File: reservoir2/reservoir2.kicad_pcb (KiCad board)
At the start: 2 copper layers, 104.1 x 66.7 mm, 2 parts

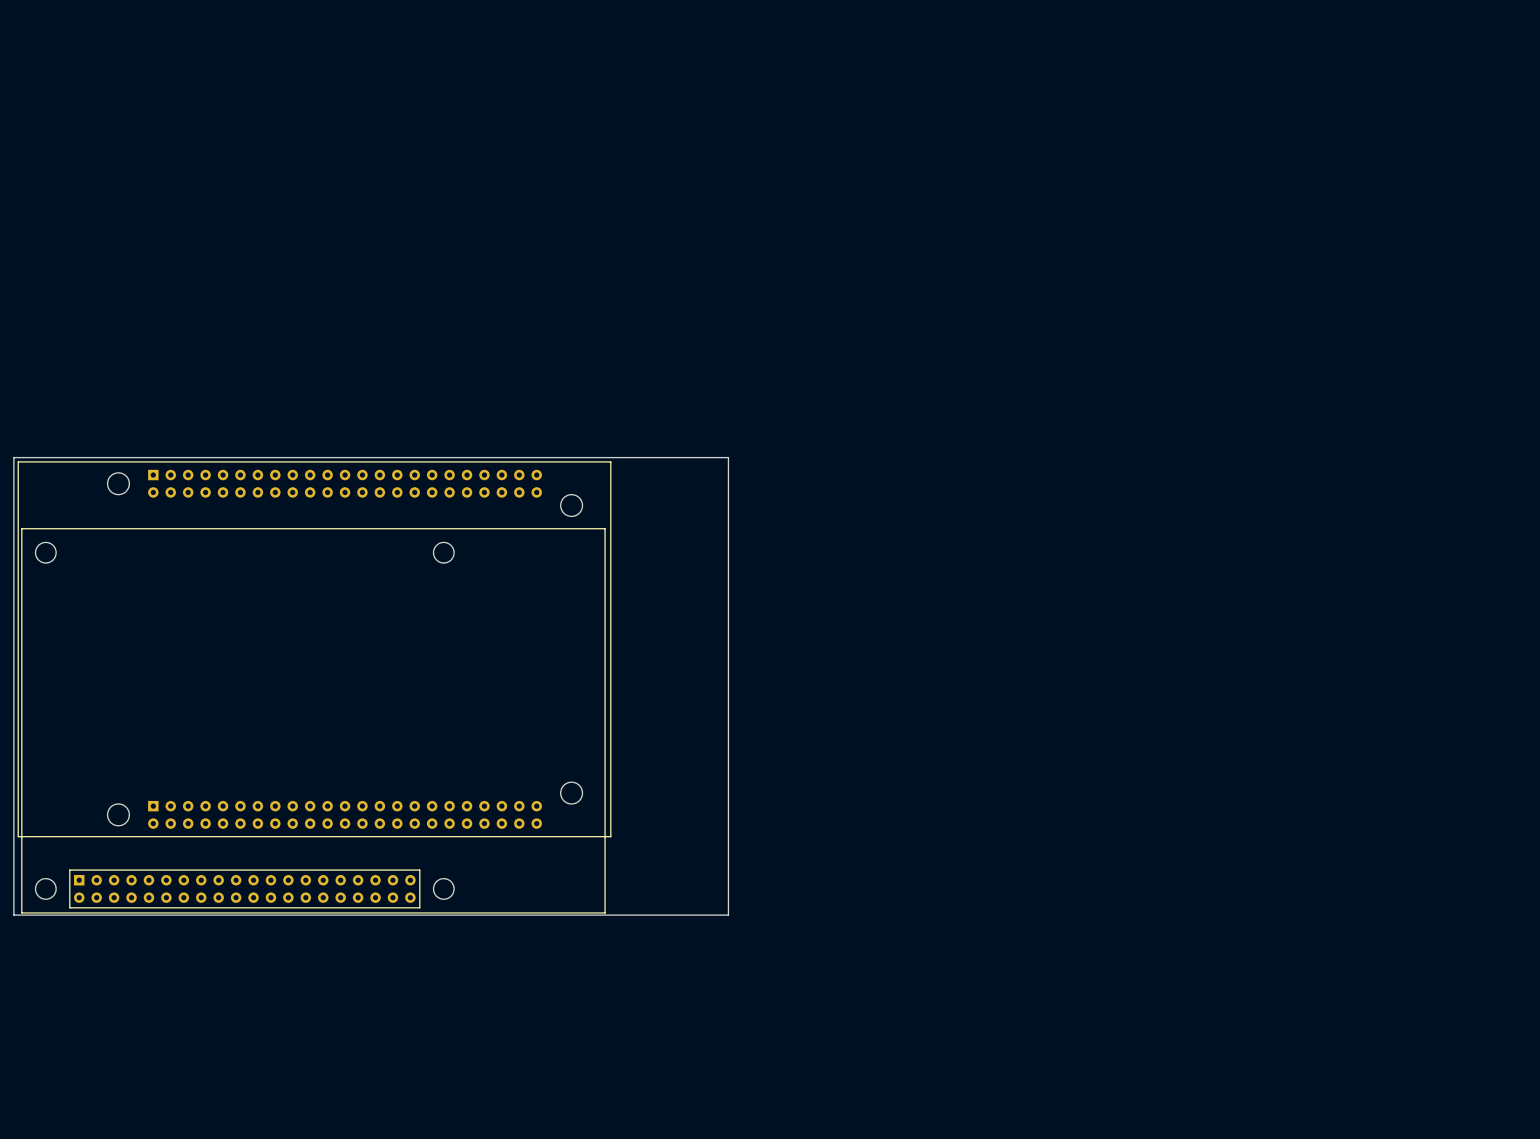
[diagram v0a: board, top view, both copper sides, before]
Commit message: Created new board design for connected grounds.
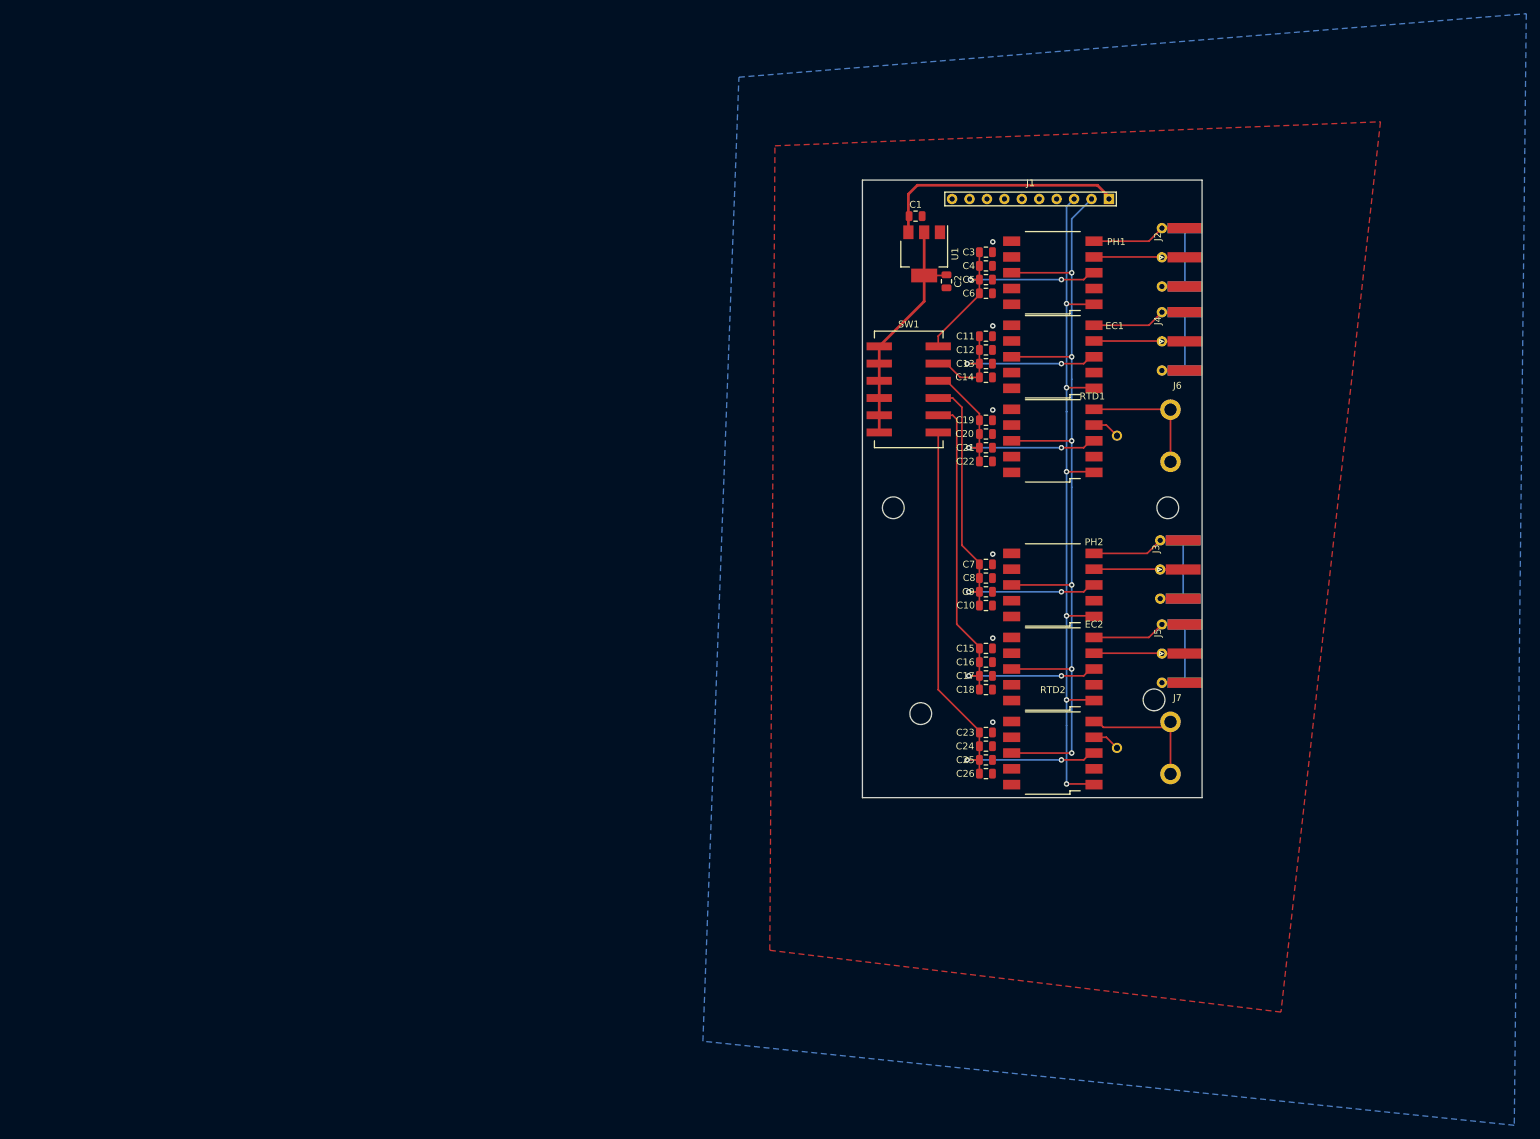
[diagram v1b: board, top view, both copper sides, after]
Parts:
- removed REF**: RaspberryPi_UpsideDown, BCR_SBC:RaspberryPi_UpsideDown
- removed REF**: BeagleBone_UpsideDown, BCR_SBC:BeagleBone_UpsideDown
- added C1: 0.1uF, Capacitor_SMD:C_0805_2012Metric, F.Cu at (208.2, 24.5)
- added C10: 0.1uF, Capacitor_SMD:C_0805_2012Metric, F.Cu at (218.5, 81.2)
- added C11: 0.1uF, Capacitor_SMD:C_0805_2012Metric, F.Cu at (218.5, 42.0)
- added C12: 0.1uF, Capacitor_SMD:C_0805_2012Metric, F.Cu at (218.5, 44.0)
- added C13: 0.1uF, Capacitor_SMD:C_0805_2012Metric, F.Cu at (218.5, 46.0)
- added C14: 0.1uF, Capacitor_SMD:C_0805_2012Metric, F.Cu at (218.5, 48.0)
- added C15: 0.1uF, Capacitor_SMD:C_0805_2012Metric, F.Cu at (218.5, 87.5)
- added C16: 0.1uF, Capacitor_SMD:C_0805_2012Metric, F.Cu at (218.5, 89.5)
- added C17: 0.1uF, Capacitor_SMD:C_0805_2012Metric, F.Cu at (218.5, 91.5)
- added C18: 0.1uF, Capacitor_SMD:C_0805_2012Metric, F.Cu at (218.5, 93.5)
- added C19: 0.1uF, Capacitor_SMD:C_0805_2012Metric, F.Cu at (218.5, 54.2)
- added C2: 0.1uF, Capacitor_SMD:C_0805_2012Metric, F.Cu at (212.8, 34.0)
- added C20: 0.1uF, Capacitor_SMD:C_0805_2012Metric, F.Cu at (218.5, 56.2)
- added C21: 0.1uF, Capacitor_SMD:C_0805_2012Metric, F.Cu at (218.5, 58.2)
- added C22: 0.1uF, Capacitor_SMD:C_0805_2012Metric, F.Cu at (218.5, 60.2)
- added C23: 0.1uF, Capacitor_SMD:C_0805_2012Metric, F.Cu at (218.5, 99.8)
- added C24: 0.1uF, Capacitor_SMD:C_0805_2012Metric, F.Cu at (218.5, 101.8)
- added C25: 0.1uF, Capacitor_SMD:C_0805_2012Metric, F.Cu at (218.5, 103.8)
- added C26: 0.1uF, Capacitor_SMD:C_0805_2012Metric, F.Cu at (218.5, 105.8)
- added C3: 0.1uF, Capacitor_SMD:C_0805_2012Metric, F.Cu at (218.5, 29.8)
- added C4: 0.1uF, Capacitor_SMD:C_0805_2012Metric, F.Cu at (218.5, 31.8)
- added C5: 0.1uF, Capacitor_SMD:C_0805_2012Metric, F.Cu at (218.5, 33.8)
- added C6: 0.1uF, Capacitor_SMD:C_0805_2012Metric, F.Cu at (218.5, 35.8)
- added C7: 0.1uF, Capacitor_SMD:C_0805_2012Metric, F.Cu at (218.5, 75.2)
- added C8: 0.1uF, Capacitor_SMD:C_0805_2012Metric, F.Cu at (218.5, 77.2)
- added C9: 0.1uF, Capacitor_SMD:C_0805_2012Metric, F.Cu at (218.5, 79.2)
- added EC1: AtlasScientific_EC, BCR_Langhe:AtlasScientific_OEM, F.Cu at (228.2, 45.0)
- added EC2: AtlasScientific_EC, BCR_Langhe:AtlasScientific_OEM, F.Cu at (228.2, 90.5)
- added J1: Conn_01x10, BCR_Langhe:Proto2_DaughterCard, F.Cu at (225.0, 22.0)
- added J2: SMA, BCR_Connector:SMA_EdgeMount, F.Cu at (247.5, 30.5)
- added J3: SMA, BCR_Connector:SMA_EdgeMount, F.Cu at (247.2, 76.0)
- added J4: SMA, BCR_Connector:SMA_EdgeMount, F.Cu at (247.5, 42.8)
- added J5: SMA, BCR_Connector:SMA_EdgeMount, F.Cu at (247.5, 88.2)
- added J6: BNC, BCR_Connector:Molex_BNC_Jack_73100, F.Cu at (245.2, 56.5)
- added J7: BNC, BCR_Connector:Molex_BNC_Jack_73100, F.Cu at (245.2, 102.0)
- added PH1: AtlasScientific_PH, BCR_Langhe:AtlasScientific_OEM, F.Cu at (228.2, 32.8)
- added PH2: AtlasScientific_PH, BCR_Langhe:AtlasScientific_OEM, F.Cu at (228.2, 78.2)
- added RTD1: AtlasScientific_RTD, BCR_Langhe:AtlasScientific_OEM, F.Cu at (228.2, 57.2)
- added RTD2: AtlasScientific_RTD, BCR_Langhe:AtlasScientific_OEM, F.Cu at (228.2, 102.8)
- added SW1: SW_DIP_x06, BCR_Switch:Cixi_SMD_DIP_Switch_6, F.Cu at (207.2, 49.8)
- added U1: AMS1117-5.0, Package_TO_SOT_SMD:SOT-223-3_TabPin2, F.Cu at (209.5, 30.0)
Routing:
- net /SCL: track 0.00 -> 134.6 mm, vias 0 -> 6
- net /SDA: track 0.00 -> 111.0 mm, vias 0 -> 6
- net /S_RTD_VCC: track 0.00 -> 72.9 mm, vias 0 -> 2
- net /S_EC_VCC: track 0.00 -> 63.9 mm, vias 0 -> 2
- net /S_PH_VCC: track 0.00 -> 54.4 mm, vias 0 -> 2
- net VDD: track 0.00 -> 36.5 mm
- net /R_PH_VCC: track 0.00 -> 35.9 mm, vias 0 -> 2
- net /R_RTD_VCC: track 0.00 -> 35.6 mm, vias 0 -> 2
- net +3V3: track 0.00 -> 35.2 mm
- net /R_EC_VCC: track 0.00 -> 33.6 mm, vias 0 -> 2
- net Net-(J2-Pad2): track 0.00 -> 33.1 mm
- net Net-(EC2-Pad5): track 0.00 -> 32.6 mm
- net Net-(EC1-Pad5): track 0.00 -> 32.6 mm
- net Net-(J3-Pad2): track 0.00 -> 32.3 mm
- net Net-(J7-Pad2): track 0.00 -> 19.4 mm
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- added copper zone on B.Cu, net GND
- added copper zone on F.Cu, net GND
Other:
- board size 104.1 x 66.7 mm -> 49.5 x 90 mm

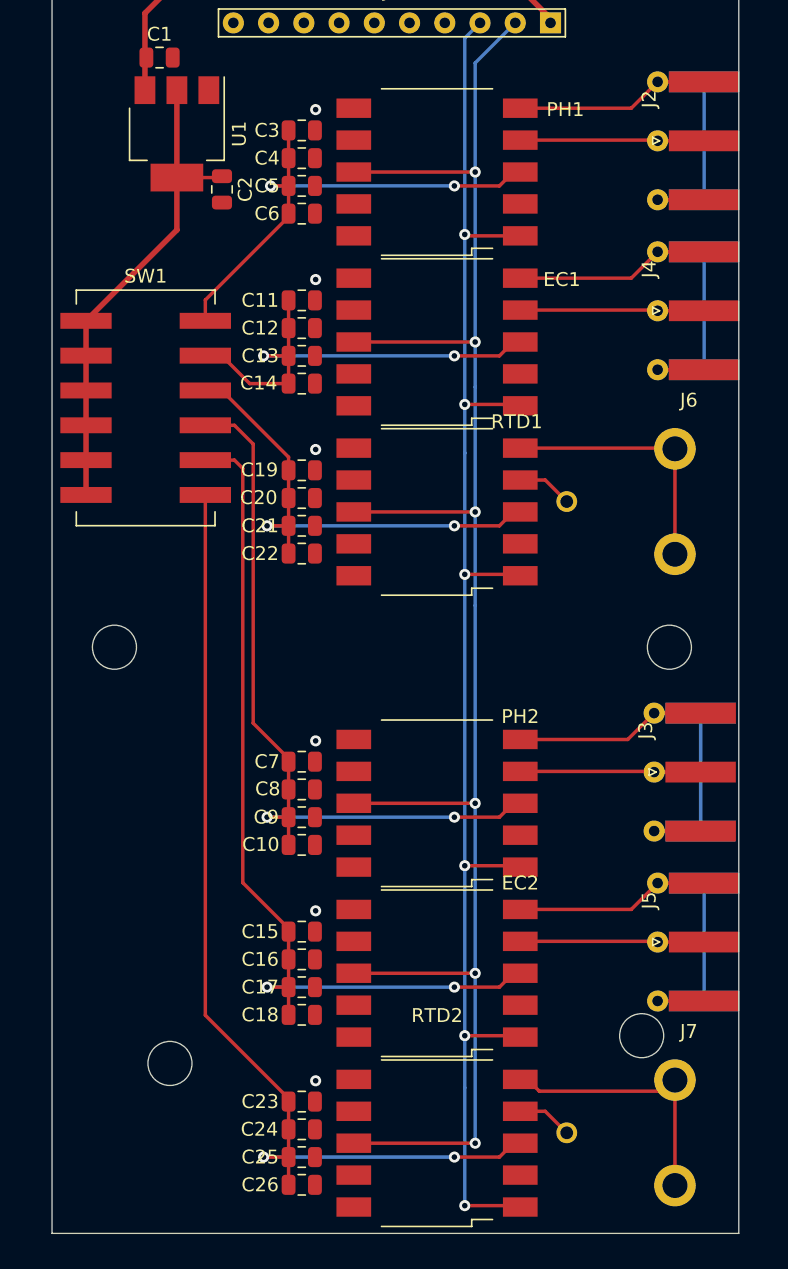
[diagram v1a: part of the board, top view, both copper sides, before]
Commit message: Updates and changes for production run of 0.1.0
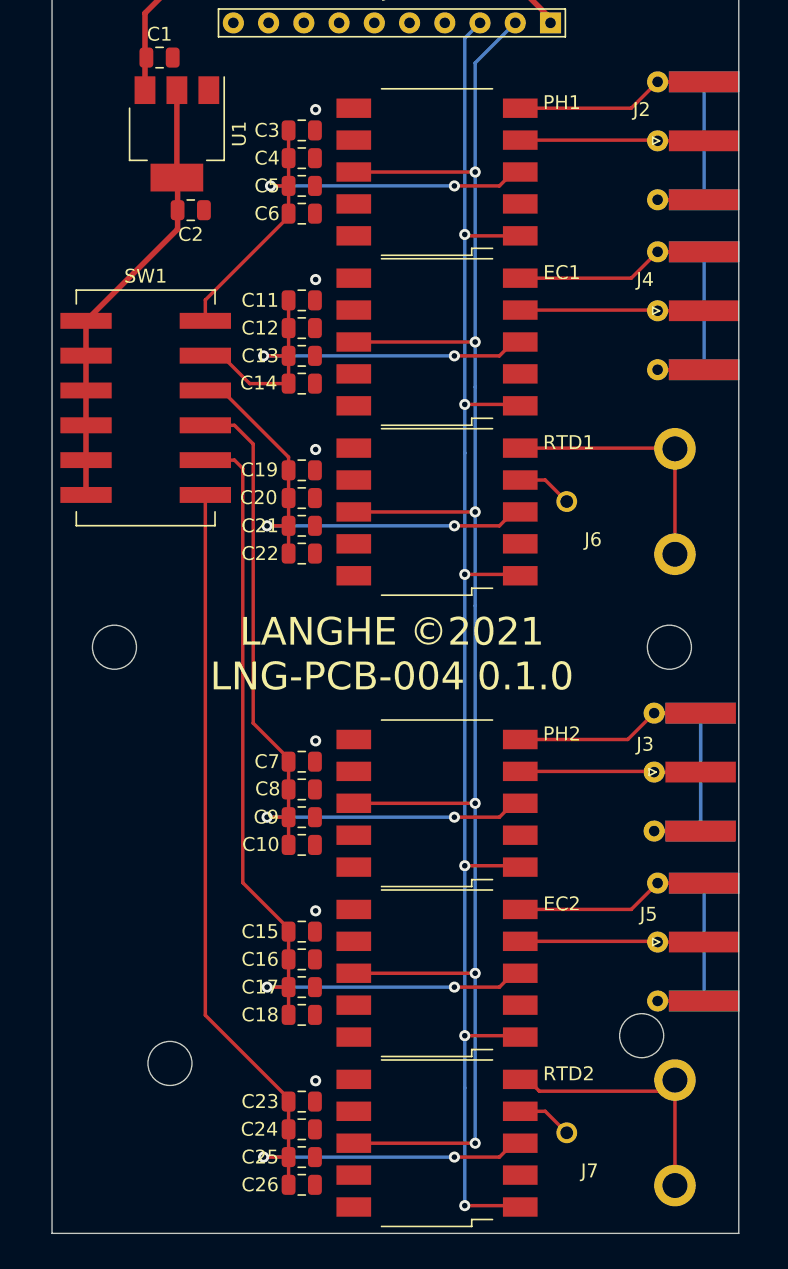
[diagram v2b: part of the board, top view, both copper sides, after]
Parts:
- moved C2 2.70 mm to (210.5, 35.5), turned to 0 degrees
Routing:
- net +3V3: track 35.2 -> 31.9 mm
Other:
- board text added: "LANGHE ©2021 LNG-PCB-004 0.1.0"

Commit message: Reworked board for just one reservoir with isolators and removed temperature.
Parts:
- removed C1, C2, C3, C4, C5, C6, C7, C8, C9: 0.1uF, Capacitor_SMD:C_0805_2012Metric
- removed EC1, EC2: AtlasScientific_EC, BCR_Langhe:AtlasScientific_OEM
- removed J2, J3, J4, J5: SMA, BCR_Connector:SMA_EdgeMount
- removed J6, J7: BNC, BCR_Connector:Molex_BNC_Jack_73100
- removed PH1, PH2: AtlasScientific_PH, BCR_Langhe:AtlasScientific_OEM
- removed RTD1, RTD2: AtlasScientific_RTD, BCR_Langhe:AtlasScientific_OEM
- removed SW1: SW_DIP_x06, BCR_Switch:Cixi_SMD_DIP_Switch_6
- removed U1: AMS1117-5.0, Package_TO_SOT_SMD:SOT-223-3_TabPin2
- added C110: 0.1uF, Capacitor_SMD:C_0805_2012Metric, F.Cu at (103.2, 67.5)
- added C210: 0.1uF, Capacitor_SMD:C_0805_2012Metric, F.Cu at (80.2, 67.4)
- added C27: 0.1uF, Capacitor_SMD:C_0805_2012Metric, F.Cu at (86.5, 86.0)
- added C28: 0.1uF, Capacitor_SMD:C_0805_2012Metric, F.Cu at (86.5, 84.0)
- added C29: 0.1uF, Capacitor_SMD:C_0805_2012Metric, F.Cu at (86.5, 82.0)
- added EC20: AtlasScientific_EC, BCR_Langhe:AtlasScientific_OEM, F.Cu at (78.5, 85.0)
- added J10: SMA, Connector_BCR:SMA_EdgeMount, F.Cu at (104.0, 97.3)
- added J20: SMA, Connector_BCR:SMA_EdgeMount, F.Cu at (81.0, 97.3)
- added L10: 6.8uH, Inductor_SMD:L_0805_2012Metric, F.Cu at (109.0, 61.5)
- added L20: 6.8uH, Inductor_SMD:L_0805_2012Metric, F.Cu at (86.0, 61.5)
- added PH10: AtlasScientific_PH, BCR_Langhe:AtlasScientific_OEM, F.Cu at (101.5, 85.0)
- added PS10: Mornsun_B0505S-1WR3, JLCPCB:Mornsun_B0505S-1WR3, F.Cu at (107.2, 66.4)
- added PS20: Mornsun_B0505S-1WR3, JLCPCB:Mornsun_B0505S-1WR3, F.Cu at (84.2, 66.4)
- added R10: 0R, Resistor_SMD:R_0805_2012Metric, F.Cu at (101.0, 64.5)
- added R11: 4.7K, Resistor_SMD:R_0805_2012Metric, F.Cu at (96.5, 75.5)
- added R12: 4.7K, Resistor_SMD:R_0805_2012Metric, F.Cu at (100.0, 75.5)
- added R20: 0R, Resistor_SMD:R_0805_2012Metric, F.Cu at (78.0, 64.5)
- added R21: 4.7K, Resistor_SMD:R_0805_2012Metric, F.Cu at (73.5, 75.5)
- added R22: 4.7K, Resistor_SMD:R_0805_2012Metric, F.Cu at (77.0, 75.5)
- added U10: Analog_ADUM1250ARZ-RL7, JLCPCB:SOIC-8_3.9x4.9mm_P1.27mm, F.Cu at (99.0, 70.0)
- added U20: Analog_ADUM1250ARZ-RL7, JLCPCB:SOIC-8_3.9x4.9mm_P1.27mm, F.Cu at (76.0, 70.0)
- C10, C11, C20, C21: value 0.1uF -> 4.7uF
- C12, C22: value 0.1uF -> 1nF
- moved C25 150.4 mm to (71.5, 72.0), turned to -90 degrees
- moved C24 148.7 mm to (74.5, 64.5), turned to 180 degrees
- moved C23 140.0 mm to (81.0, 73.5), turned to 90 degrees
- moved J1 135.5 mm to (92.5, 50.5)
- moved C21 135.0 mm to (83.5, 61.5), turned to 90 degrees
- moved C26 133.2 mm to (86.5, 88.0)
- moved C20 130.6 mm to (88.0, 61.5), turned to -90 degrees
- moved C22 127.9 mm to (91.0, 70.0), turned to -90 degrees
- moved C15 125.0 mm to (94.5, 72.0), turned to -90 degrees
- moved C14 122.1 mm to (97.5, 64.5), turned to 180 degrees
- moved C13 117.8 mm to (104.0, 73.5), turned to 90 degrees
- moved C19 114.1 mm to (109.5, 88.0)
- moved C11 113.2 mm to (107.0, 61.5), turned to 90 degrees
- moved C10 109.3 mm to (111.0, 61.5), turned to -90 degrees
- moved C16 109.3 mm to (109.5, 82.0)
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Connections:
- C10 pad 1: /S_PH_VCC -> VDD
- C11 pad 1: /R_EC_VCC -> Net-(C11-Pad1)
- C12 pad 1: /R_EC_VCC -> GND
- C12 pad 2: GND -> /GND_PH
- C13 pad 1: /R_EC_VCC -> /VDD_PH
- C13 pad 2: GND -> /GND_PH
- C14 pad 1: /R_EC_VCC -> Net-(C14-Pad1)
- C15 pad 1: /S_EC_VCC -> /VDD_PH
- C15 pad 2: GND -> /GND_PH
- C16 pad 1: /S_EC_VCC -> /VDD_PH
- C16 pad 2: GND -> /GND_PH
- C17 pad 1: /S_EC_VCC -> /VDD_PH
- C17 pad 2: GND -> /GND_PH
- C18 pad 1: /S_EC_VCC -> /VDD_PH
- C18 pad 2: GND -> /GND_PH
- C19 pad 1: /R_RTD_VCC -> /VDD_PH
- C19 pad 2: GND -> /GND_PH
- C20 pad 1: /R_RTD_VCC -> VDD
- C21 pad 1: /R_RTD_VCC -> Net-(C21-Pad1)
- C22 pad 1: /R_RTD_VCC -> GND
- C22 pad 2: GND -> /GND_EC
- C23 pad 1: /S_RTD_VCC -> /VDD_EC
- C23 pad 2: GND -> /GND_EC
- C24 pad 1: /S_RTD_VCC -> Net-(C24-Pad1)
- C25 pad 1: /S_RTD_VCC -> /VDD_EC
- C25 pad 2: GND -> /GND_EC
- C26 pad 1: /S_RTD_VCC -> /VDD_EC
- C26 pad 2: GND -> /GND_EC
- J1 pad 4: Net-(J1-Pad4) -> unconnected-(J1-Pad4)
- J1 pad 5: Net-(J1-Pad5) -> unconnected-(J1-Pad5)
- J1 pad 6: Net-(J1-Pad6) -> unconnected-(J1-Pad6)
- J1 pad 7: Net-(J1-Pad7) -> unconnected-(J1-Pad7)
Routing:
- net /S_RTD_VCC: track 72.9 -> 0.00 mm, vias 2 -> 0
- net /SCL: track 134.6 -> 63.3 mm, vias 6 -> 3
- net /S_EC_VCC: track 63.9 -> 0.00 mm, vias 2 -> 0
- net /SDA: track 111.0 -> 56.5 mm, vias 6 -> 3
- net /S_PH_VCC: track 54.4 -> 0.00 mm, vias 2 -> 0
- net /R_PH_VCC: track 35.9 -> 0.00 mm, vias 2 -> 0
- net /R_RTD_VCC: track 35.6 -> 0.00 mm, vias 2 -> 0
- net /R_EC_VCC: track 33.6 -> 0.00 mm, vias 2 -> 0
- net Net-(J2-Pad2): track 33.1 -> 0.00 mm
- net Net-(EC2-Pad5): track 32.6 -> 0.00 mm
- net Net-(EC1-Pad5): track 32.6 -> 0.00 mm
- net Net-(J3-Pad2): track 32.3 -> 0.00 mm
- net +3V3: track 31.9 -> 0.00 mm
- net VDD: track 36.5 -> 6.13 mm, vias 0 -> 4
- net /VDD_PH: track 0.00 -> 25.4 mm, vias 0 -> 5
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- added copper zone on F.Cu, net /GND_EC
- added copper zone on F.Cu, net /GND_PH
- added copper zone on B.Cu, net /VDD_EC
- added copper zone on B.Cu, net /VDD_PH
- added copper zone on B.Cu, net VDD
- removed copper zone on B.Cu, net GND
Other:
- board size 49.5 x 90 mm -> 49.5 x 52.2 mm
- net class Default removed
- board text removed: "LANGHE ©2021 LNG-PCB-004 0.1.0"
